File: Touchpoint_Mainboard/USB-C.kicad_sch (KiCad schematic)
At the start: 8 parts, among them J1 USB4105-GF-A, U2 USBLC6-2SC6

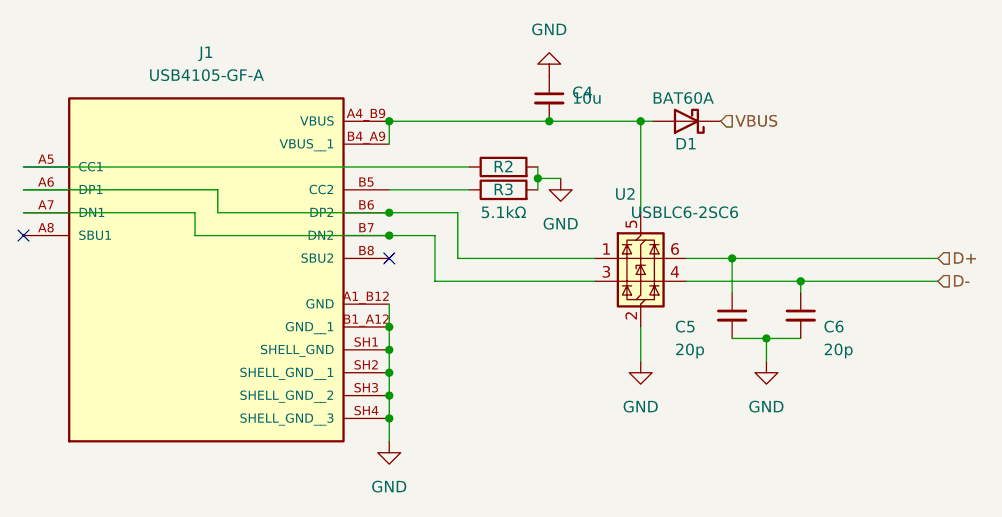
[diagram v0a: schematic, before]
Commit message: FInished populating mainboard schematic
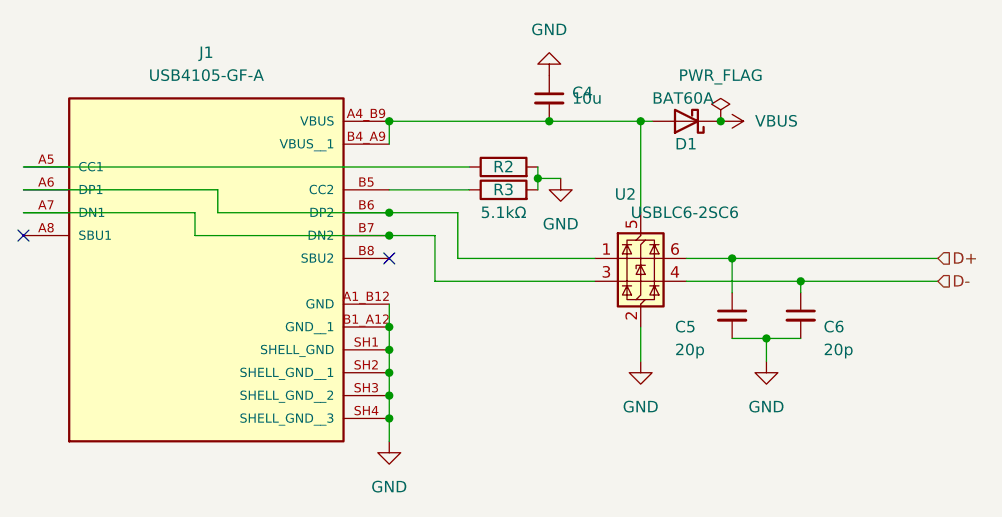
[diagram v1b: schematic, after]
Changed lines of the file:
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@@
+	)
+	(junction
+		(at 109.22 39.37)
+		(diameter 0)
+		(color 0 0 0 0)
 	)
 	(junction
@@
 		(shape input)
 		(at 133.35 57.15 0)
-		(effects
-			(font
-				(size 1.27 1.27)
-			)
-			(justify left)
-		)
-	)
-	(hierarchical_label "VBUS"
-		(shape input)
-		(at 109.22 39.37 0)
 		(effects
 			(font
@@
 					(unit 1)
 				)
+			)
+		)
+	)
+	(symbol
+		(lib_id "power:PWR_FLAG")
+		(at 109.22 39.37 0)
+		(unit 1)
+		(exclude_from_sim no)
+		(in_bom yes)
+		(on_board yes)
+		(dnp no)
+		(fields_autoplaced yes)
+		(property "Reference" "#FLG01"
+			(at 109.22 37.465 0)
+			(effects
+				(font
+					(size 1.27 1.27)
+				)
+				(hide yes)
+			)
+		)
+		(property "Value" "PWR_FLAG"
+			(at 109.22 34.29 0)
+			(effects
+				(font
+					(size 1.27 1.27)
+				)
+			)
+		)
+		(property "Footprint" ""
+			(at 109.22 39.37 0)
+			(effects
+				(font
+					(size 1.27 1.27)
+				)
+				(hide yes)
+			)
+		)
+		(property "Datasheet" "~"
+			(at 109.22 39.37 0)
+			(effects
+				(font
+					(size 1.27 1.27)
+				)
+				(hide yes)
+			)
+		)
+		(property "Description" "Special symbol for telling ERC where power comes from"
+			(at 109.22 39.37 0)
+			(effects
+				(font
+					(size 1.27 1.27)
+				)
+				(hide yes)
+			)
+		)
+		(pin "1"
+		)
+		(instances
+			(project ""
+				(path "/f37b5f88-420a-4646-85df-8f9851d23e3c/4f170ae2-2af9-4cae-a958-9ac1ab5fab2b"
+					(reference "#FLG01")
+					(unit 1)
+				)
+			)
+		)
+	)
+	(symbol
+		(lib_id "power:VBUS")
+		(at 109.22 39.37 270)
+		(unit 1)
+		(exclude_from_sim no)
+		(in_bom yes)
+		(on_board yes)
+		(dnp no)
+		(fields_autoplaced yes)
+		(property "Reference" "#PWR04"
+			(at 105.41 39.37 0)
+			(effects
+				(font
+					(size 1.27 1.27)
+				)
+				(hide yes)
+			)
+		)
+		(property "Value" "VBUS"
+			(at 113.03 39.3699 90)
+			(effects
+				(font
+					(size 1.27 1.27)
+				)
+				(justify left)
+			)
+		)
+		(property "Footprint" ""
+			(at 109.22 39.37 0)
+			(effects
+				(font
+					(size 1.27 1.27)
+				)
+				(hide yes)
+			)
+		)
+		(property "Datasheet" ""
+			(at 109.22 39.37 0)
+			(effects
+				(font
+					(size 1.27 1.27)
+				)
+				(hide yes)
+			)
+		)
+		(property "Description" "Power symbol creates a global label with name \"VBUS\""
+			(at 109.22 39.37 0)
+			(effects
+				(font
+					(size 1.27 1.27)
+				)
+				(hide yes)
+			)
+		)
+		(pin "1"
+		)
+		(instances
+			(project ""
+				(path "/f37b5f88-420a-4646-85df-8f9851d23e3c/4f170ae2-2af9-4cae-a958-9ac1ab5fab2b"
+					(reference "#PWR04")
+					(unit 1)
+				)

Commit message: Added 3.3V to interface
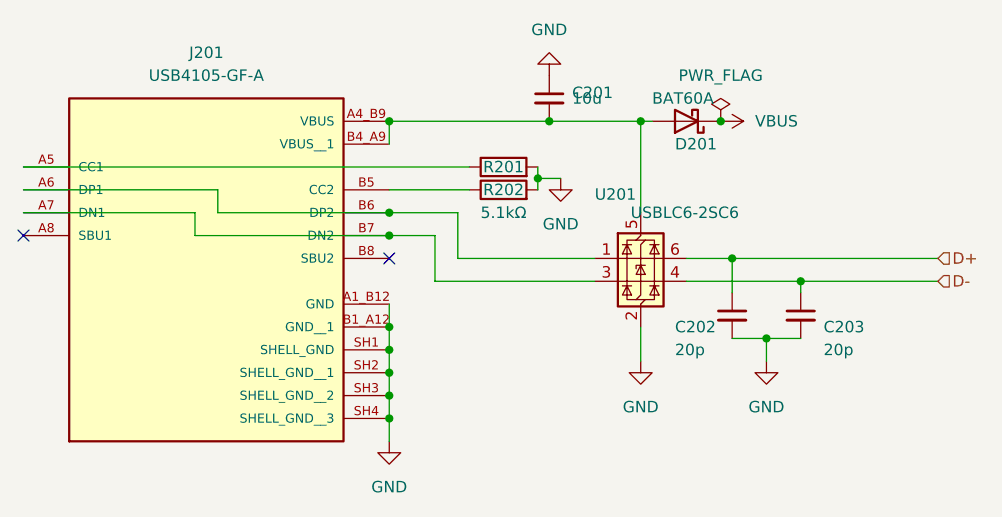
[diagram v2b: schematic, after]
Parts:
- renumbered C4 to C201, C5 to C202, C6 to C203, D1 to D201, J1 to J201, R2 to R201, R3 to R202, U2 to U201
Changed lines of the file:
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@@
 		(on_board yes)
 		(dnp no)
-		(property "Reference" "C4"
+		(property "Reference" "C201"
 			(at 92.71 36.2013 0)
 			(effects
@@
 			(project "Touchpoint_Mainboard"
 				(path "/f37b5f88-420a-4646-85df-8f9851d23e3c/4f170ae2-2af9-4cae-a958-9ac1ab5fab2b"
-					(reference "C4")
+					(reference "C201")
 					(unit 1)
 				)
@@
 		(dnp no)
 		(fields_autoplaced yes)
-		(property "Reference" "#PWR09"
+		(property "Reference" "#PWR0203"
 			(at 91.44 52.07 0)
 			(effects
@@
 			(project "Touchpoint_Mainboard"
 				(path "/f37b5f88-420a-4646-85df-8f9851d23e3c/4f170ae2-2af9-4cae-a958-9ac1ab5fab2b"
-					(reference "#PWR09")
+					(reference "#PWR0203")
 					(unit 1)
 				)
@@
 		(dnp no)
 		(fields_autoplaced yes)
-		(property "Reference" "J1"
+		(property "Reference" "J201"
 			(at 52.07 31.75 0)
 			(effects
@@
 			(project "Touchpoint_Mainboard"
 				(path "/f37b5f88-420a-4646-85df-8f9851d23e3c/4f170ae2-2af9-4cae-a958-9ac1ab5fab2b"
-					(reference "J1")
+					(reference "J201")
 					(unit 1)
 				)
@@
 		(on_board yes)
 		(dnp no)
-		(property "Reference" "R3"
+		(property "Reference" "R202"
 			(at 85.09 46.99 90)
 			(effects
@@
 			(project "Touchpoint_Mainboard"
 				(path "/f37b5f88-420a-4646-85df-8f9851d23e3c/4f170ae2-2af9-4cae-a958-9ac1ab5fab2b"
-					(reference "R3")
+					(reference "R202")
 					(unit 1)
 				)
@@
 		(on_board yes)
 		(dnp no)
-		(property "Reference" "U2"
+		(property "Reference" "U201"
 			(at 99.822 47.498 0)
 			(effects
@@
 			(project "Touchpoint_Mainboard"
 				(path "/f37b5f88-420a-4646-85df-8f9851d23e3c/4f170ae2-2af9-4cae-a958-9ac1ab5fab2b"
-					(reference "U2")
+					(reference "U201")
 					(unit 1)
 				)
@@
 		(on_board yes)
 		(dnp no)
-		(property "Reference" "R2"
+		(property "Reference" "R201"
 			(at 85.09 44.45 90)
 			(effects
@@
 			(project "Touchpoint_Mainboard"
 				(path "/f37b5f88-420a-4646-85df-8f9851d23e3c/4f170ae2-2af9-4cae-a958-9ac1ab5fab2b"
-					(reference "R2")
+					(reference "R201")
 					(unit 1)
 				)
@@
 		(dnp no)
 		(fields_autoplaced yes)
-		(property "Reference" "#PWR013"
+		(property "Reference" "#PWR0206"
 			(at 114.3 72.39 0)
 			(effects
@@
 			(project "Touchpoint_Mainboard"
 				(path "/f37b5f88-420a-4646-85df-8f9851d23e3c/4f170ae2-2af9-4cae-a958-9ac1ab5fab2b"
-					(reference "#PWR013")
+					(reference "#PWR0206")
 					(unit 1)
 				)
@@
 		(on_board yes)
 		(dnp no)
-		(property "Reference" "C5"
+		(property "Reference" "C202"
 			(at 104.14 62.23 0)
 			(effects
@@
 			(project "Touchpoint_Mainboard"
 				(path "/f37b5f88-420a-4646-85df-8f9851d23e3c/4f170ae2-2af9-4cae-a958-9ac1ab5fab2b"
-					(reference "C5")
+					(reference "C202")
 					(unit 1)
 				)
@@
 		(dnp no)
 		(fields_autoplaced yes)
-		(property "Reference" "#FLG01"
+		(property "Reference" "#FLG0201"
 			(at 109.22 37.465 0)
 			(effects
@@
 			(project ""
 				(path "/f37b5f88-420a-4646-85df-8f9851d23e3c/4f170ae2-2af9-4cae-a958-9ac1ab5fab2b"
-					(reference "#FLG01")
+					(reference "#FLG0201")
 					(unit 1)
 				)
@@
 		(dnp no)
 		(fields_autoplaced yes)
-		(property "Reference" "#PWR04"
+		(property "Reference" "#PWR0205"
 			(at 105.41 39.37 0)
 			(effects
@@
 			(project ""
 				(path "/f37b5f88-420a-4646-85df-8f9851d23e3c/4f170ae2-2af9-4cae-a958-9ac1ab5fab2b"
-					(reference "#PWR04")
+					(reference "#PWR0205")
 					(unit 1)
 				)
@@
 		(on_board yes)
 		(dnp no)
-		(property "Reference" "C6"
+		(property "Reference" "C203"
 			(at 120.65 62.23 0)
 			(effects
@@
 			(project "Touchpoint_Mainboard"
 				(path "/f37b5f88-420a-4646-85df-8f9851d23e3c/4f170ae2-2af9-4cae-a958-9ac1ab5fab2b"
-					(reference "C6")
+					(reference "C203")
 					(unit 1)
 				)
@@
 		(dnp no)
 		(fields_autoplaced yes)
-		(property "Reference" "#PWR07"
+		(property "Reference" "#PWR0201"
 			(at 72.39 81.28 0)
 			(effects
@@
 			(project "Touchpoint_Mainboard"
 				(path "/f37b5f88-420a-4646-85df-8f9851d23e3c/4f170ae2-2af9-4cae-a958-9ac1ab5fab2b"
-					(reference "#PWR07")
+					(reference "#PWR0201")
 					(unit 1)
 				)
@@
 		(dnp no)
 		(fields_autoplaced yes)
-		(property "Reference" "#PWR011"
+		(property "Reference" "#PWR0204"
 			(at 100.33 72.39 0)
 			(effects
@@
 			(project "Touchpoint_Mainboard"
 				(path "/f37b5f88-420a-4646-85df-8f9851d23e3c/4f170ae2-2af9-4cae-a958-9ac1ab5fab2b"
-					(reference "#PWR011")
+					(reference "#PWR0204")
 					(unit 1)
 				)
@@
 		(on_board yes)
 		(dnp no)
-		(property "Reference" "D1"
+		(property "Reference" "D201"
 			(at 104.14 41.91 0)
 			(effects
@@
 			(project "Touchpoint_Mainboard"
 				(path "/f37b5f88-420a-4646-85df-8f9851d23e3c/4f170ae2-2af9-4cae-a958-9ac1ab5fab2b"
-					(reference "D1")
+					(reference "D201")
 					(unit 1)
 				)
@@
 		(dnp no)
 		(fields_autoplaced yes)
-		(property "Reference" "#PWR08"
+		(property "Reference" "#PWR0202"
 			(at 90.17 27.94 0)
 			(effects
@@
 			(project "Touchpoint_Mainboard"
 				(path "/f37b5f88-420a-4646-85df-8f9851d23e3c/4f170ae2-2af9-4cae-a958-9ac1ab5fab2b"
-					(reference "#PWR08")
-					(unit 1)
-				)
+					(reference "#PWR0202")
+					(unit 1)
+				)
